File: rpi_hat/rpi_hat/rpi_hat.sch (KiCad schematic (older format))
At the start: 17 parts, among them J1 Raspberry_Pi_2_3, J2 Screw_Terminal_01x02, J3 Screw_Terminal_01x02, J4 Screw_Terminal_01x02, J5 Screw_Terminal_01x02, Q1 2SC1815, Q2 2N7000, U1 L7805

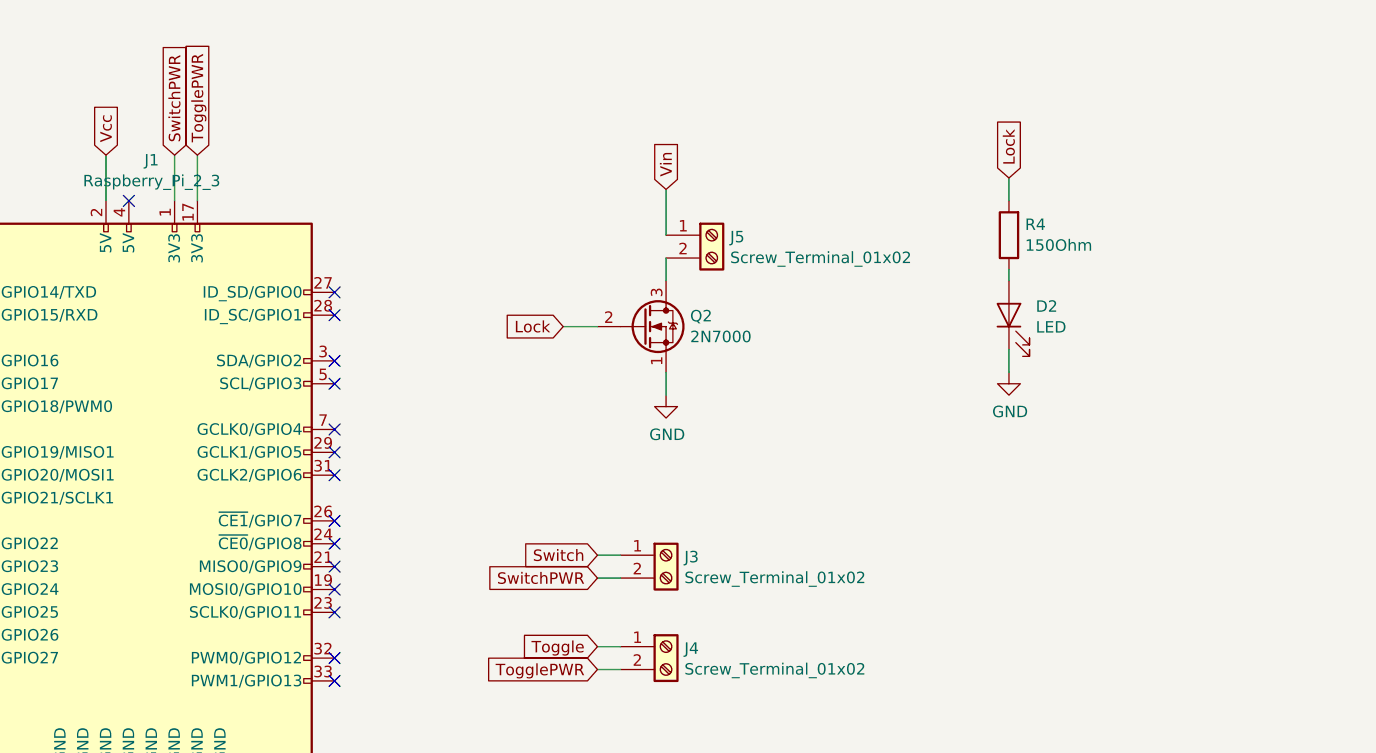
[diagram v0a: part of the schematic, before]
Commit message: Fix pushbutton switch circuit so it doesn't rely on the Pi working
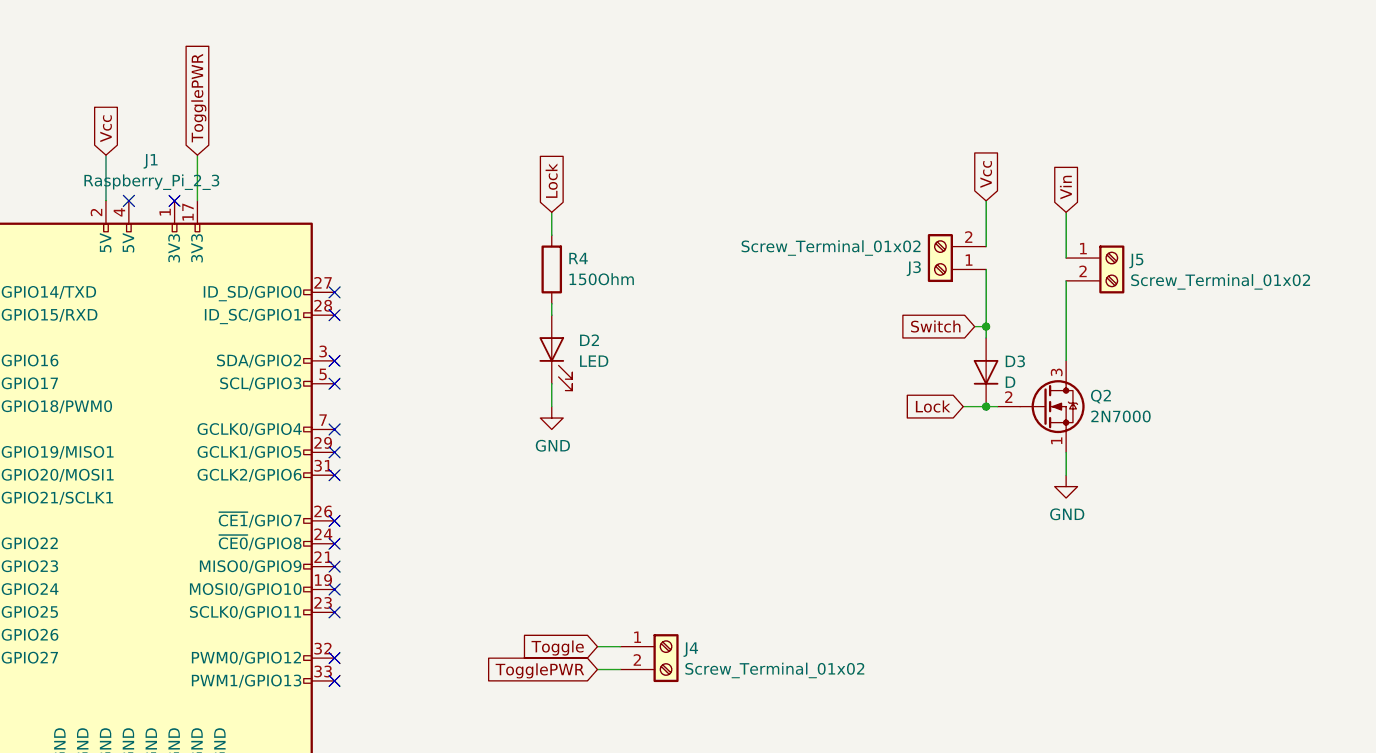
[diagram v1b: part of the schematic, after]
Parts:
- added D3: D, Diodes_SMD:SOD-123, symbol Device:D
- J1: Digikey # (none) -> 1528-1785-ND
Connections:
- net Lock: now also D3.1 (K)
- net Switch: now also D3.2 (A)
- net Vcc: now also J3.2 (Pin_2)
- net SwitchPWR: no longer names the net of J1.1 (3V3)
- net SwitchPWR: no longer J3.2 (Pin_2)
- no-connect marks 25 -> 26
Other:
- moved on the sheet: D2, J3, J5, Q2, R4
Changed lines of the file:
@@
 EESchema Schematic File Version 4
+LIBS:rpi_hat-cache
 EELAYER 26 0
 EELAYER END
@@
 F 2 "Pin_Headers:Pin_Header_Straight_2x20" H 5250 3500 50  0001 C CNN
 F 3 "https://www.raspberrypi.org/documentation/hardware/raspberrypi/schematics/rpi_SCH_3bplus_1p0_reduced.pdf" H 5250 3500 50  0001 C CNN
+F 4 "1528-1785-ND" H 5250 3500 50  0001 C CNN "Digikey #"
 	1    5250 3500
 	1    0    0    -1
@@
 L Transistor_FET:2N7000 Q2
 U 1 1 5C747739
-P 7400 2750
-F 0 "Q2" H 7605 2796 50  0000 L CNN
-F 1 "2N7000" H 7605 2705 50  0000 L CNN
-F 2 "TO_SOT_Packages_THT:TO-220_Neutral123_Horizontal" H 7600 2675 50  0001 L CIN
-F 3 "https://www.fairchildsemi.com/datasheets/2N/2N7000.pdf" H 7400 2750 50  0001 L CNN
-F 4 "497-2779-5-ND" H 7400 2750 50  0001 C CNN "Digikey #"
-	1    7400 2750
-	1    0    0    -1
-$EndComp
-Text GLabel 7050 2750 0    50   Input ~ 0
+P 9150 3100
+F 0 "Q2" H 9355 3146 50  0000 L CNN
+F 1 "2N7000" H 9355 3055 50  0000 L CNN
+F 2 "TO_SOT_Packages_THT:TO-220_Neutral123_Horizontal" H 9350 3025 50  0001 L CIN
+F 3 "https://www.fairchildsemi.com/datasheets/2N/2N7000.pdf" H 9150 3100 50  0001 L CNN
+F 4 "497-2779-5-ND" H 9150 3100 50  0001 C CNN "Digikey #"
+	1    9150 3100
+	1    0    0    -1
+$EndComp
+Text GLabel 8800 3100 0    50   Input ~ 0
 Lock
-Wire Wire Line
-	7050 2750 7200 2750
 Text GLabel 4300 4200 0    50   Input ~ 0
 Lock
 Wire Wire Line
 	4300 4200 4450 4200
-Text GLabel 7500 2150 1    50   Input ~ 0
+Text GLabel 9250 2250 1    50   Input ~ 0
 Vin
 $Comp
 L power:GND #PWR0104
 U 1 1 5C747BD6
-P 7500 3050
-F 0 "#PWR0104" H 7500 2800 50  0001 C CNN
-F 1 "GND" H 7505 2877 50  0000 C CNN
-F 2 "" H 7500 3050 50  0001 C CNN
-F 3 "" H 7500 3050 50  0001 C CNN
-	1    7500 3050
-	1    0    0    -1
-$EndComp
-Wire Wire Line
-	7500 2950 7500 3050
+P 9250 3400
+F 0 "#PWR0104" H 9250 3150 50  0001 C CNN
+F 1 "GND" H 9255 3227 50  0000 C CNN
+F 2 "" H 9250 3400 50  0001 C CNN
+F 3 "" H 9250 3400 50  0001 C CNN
+	1    9250 3400
+	1    0    0    -1
+$EndComp
 $Comp
 L Connector:Screw_Terminal_01x02 J5
 U 1 1 5C747DD7
-P 7700 2350
-F 0 "J5" H 7780 2342 50  0000 L CNN
-F 1 "Screw_Terminal_01x02" H 7780 2251 50  0000 L CNN
-F 2 "Terminal_Blocks:TerminalBlock_Pheonix_MKDS1.5-2pol" H 7700 2350 50  0001 C CNN
-F 3 "~" H 7700 2350 50  0001 C CNN
-F 4 "277-1667-ND" H 7700 2350 50  0001 C CNN "Digikey #"
-	1    7700 2350
-	1    0    0    -1
-$EndComp
-Wire Wire Line
-	7500 2150 7500 2350
-Wire Wire Line
-	7500 2450 7500 2550
-$Comp
-L Connector:Screw_Terminal_01x02 J3
-U 1 1 5C7482A2
-P 7500 3750
-F 0 "J3" H 7580 3742 50  0000 L CNN
-F 1 "Screw_Terminal_01x02" H 7580 3651 50  0000 L CNN
-F 2 "Terminal_Blocks:TerminalBlock_Pheonix_MKDS1.5-2pol" H 7500 3750 50  0001 C CNN
-F 3 "~" H 7500 3750 50  0001 C CNN
-F 4 "277-1667-ND" H 7500 3750 50  0001 C CNN "Digikey #"
-	1    7500 3750
-	1    0    0    -1
-$EndComp
-Text GLabel 7200 3750 0    50   Input ~ 0
-Switch
-Text GLabel 7200 3850 0    50   Input ~ 0
-SwitchPWR
-Wire Wire Line
-	7200 3750 7300 3750
-Wire Wire Line
-	7300 3850 7200 3850
+P 9450 2450
+F 0 "J5" H 9530 2442 50  0000 L CNN
+F 1 "Screw_Terminal_01x02" H 9530 2351 50  0000 L CNN
+F 2 "Terminal_Blocks:TerminalBlock_Pheonix_MKDS1.5-2pol" H 9450 2450 50  0001 C CNN
+F 3 "~" H 9450 2450 50  0001 C CNN
+F 4 "277-1667-ND" H 9450 2450 50  0001 C CNN "Digikey #"
+	1    9450 2450
+	1    0    0    -1
+$EndComp
+Wire Wire Line
+	9250 2250 9250 2450
 Text GLabel 4300 4000 0    50   Input ~ 0
 Switch
 Wire Wire Line
 	4300 4000 4450 4000
-Text GLabel 5350 2000 1    50   Input ~ 0
-SwitchPWR
-Wire Wire Line
-	5350 2200 5350 2000
 $Comp
 L Connector:Screw_Terminal_01x02 J4
@@
 L Device:LED D2
 U 1 1 5C74A07C
-P 9000 2700
-F 0 "D2" V 9038 2583 50  0000 R CNN
-F 1 "LED" V 8947 2583 50  0000 R CNN
-F 2 "LEDs:LED_0603" H 9000 2700 50  0001 C CNN
-F 3 "~" H 9000 2700 50  0001 C CNN
-F 4 "160-1478-1-ND" V 9000 2700 50  0001 C CNN "Digikey #"
-	1    9000 2700
+P 7000 2850
+F 0 "D2" V 7038 2733 50  0000 R CNN
+F 1 "LED" V 6947 2733 50  0000 R CNN
+F 2 "LEDs:LED_0603" H 7000 2850 50  0001 C CNN
+F 3 "~" H 7000 2850 50  0001 C CNN
+F 4 "160-1478-1-ND" V 7000 2850 50  0001 C CNN "Digikey #"
+	1    7000 2850
 	0    -1   -1   0
 $EndComp
@@
 L Device:R R4
 U 1 1 5C74A0F2
-P 9000 2350
-F 0 "R4" H 8930 2304 50  0000 R CNN
-F 1 "150Ohm" H 8930 2395 50  0000 R CNN
-F 2 "Resistors_SMD:R_0603" V 8930 2350 50  0001 C CNN
-F 3 "~" H 9000 2350 50  0001 C CNN
-F 4 "P150DBCT-ND" H 9000 2350 50  0001 C CNN "Digikey #"
-	1    9000 2350
+P 7000 2500
+F 0 "R4" H 6930 2454 50  0000 R CNN
+F 1 "150Ohm" H 6930 2545 50  0000 R CNN
+F 2 "Resistors_SMD:R_0603" V 6930 2500 50  0001 C CNN
+F 3 "~" H 7000 2500 50  0001 C CNN
+F 4 "P150DBCT-ND" H 7000 2500 50  0001 C CNN "Digikey #"
+	1    7000 2500
 	-1   0    0    1
 $EndComp
 Wire Wire Line
-	9000 2550 9000 2500
+	7000 2700 7000 2650
 $Comp
 L power:GND #PWR0105
 U 1 1 5C74B314
-P 9000 2950
-F 0 "#PWR0105" H 9000 2700 50  0001 C CNN
-F 1 "GND" H 9005 2777 50  0000 C CNN
-F 2 "" H 9000 2950 50  0001 C CNN
-F 3 "" H 9000 2950 50  0001 C CNN
-	1    9000 2950
-	1    0    0    -1
-$EndComp
-Wire Wire Line
-	9000 2950 9000 2850
-Text GLabel 9000 2100 1    50   Input ~ 0
+P 7000 3100
+F 0 "#PWR0105" H 7000 2850 50  0001 C CNN
+F 1 "GND" H 7005 2927 50  0000 C CNN
+F 2 "" H 7000 3100 50  0001 C CNN
+F 3 "" H 7000 3100 50  0001 C CNN
+	1    7000 3100
+	1    0    0    -1
+$EndComp
+Wire Wire Line
+	7000 3100 7000 3000
+Text GLabel 7000 2250 1    50   Input ~ 0
 Lock
 Wire Wire Line
-	9000 2100 9000 2200
+	7000 2250 7000 2350
 $Comp
 L Device:Speaker LS1
@@
 NoConn ~ 6050 2600
 NoConn ~ 5150 2200
+Wire Wire Line
+	9250 2550 9250 2900
+NoConn ~ 5350 2200
+$Comp
+L Connector:Screw_Terminal_01x02 J3
+U 1 1 5C7482A2
+P 8700 2500
+F 0 "J3" H 8780 2492 50  0000 L CNN
+F 1 "Screw_Terminal_01x02" H 8780 2401 50  0000 L CNN
+F 2 "Terminal_Blocks:TerminalBlock_Pheonix_MKDS1.5-2pol" H 8700 2500 50  0001 C CNN
+F 3 "~" H 8700 2500 50  0001 C CNN
+F 4 "277-1667-ND" H 8700 2500 50  0001 C CNN "Digikey #"
+	1    8700 2500
+	-1   0    0    1
+$EndComp
+Wire Wire Line
+	9250 3300 9250 3400
+Wire Wire Line
+	8900 2500 8900 2750
+Text GLabel 8850 2750 0    50   Input ~ 0
+Switch
+Wire Wire Line
+	8850 2750 8900 2750
+Text GLabel 8900 2200 1    50   Input ~ 0
+Vcc
+Wire Wire Line
+	8900 2200 8900 2400
+Wire Wire Line
+	8800 3100 8900 3100
+$Comp
+L Device:D D3
+U 1 1 5C76DE1A
+P 8900 2950
+F 0 "D3" V 8946 2871 50  0000 R CNN
+F 1 "D" V 8855 2871 50  0000 R CNN
+F 2 "Diodes_SMD:SOD-123" H 8900 2950 50  0001 C CNN
+F 3 "~" H 8900 2950 50  0001 C CNN
+F 4 "1N4148WTPMSCT-ND" V 8900 2950 50  0001 C CNN "Digikey #"
+	1    8900 2950
+	0    -1   -1   0
+$EndComp
+Wire Wire Line
+	8900 2800 8900 2750
+Connection ~ 8900 2750
+Connection ~ 8900 3100
+Wire Wire Line
+	8900 3100 8950 3100
 $EndSCHEMATC

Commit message: Correct digikey part # for piezo transistor
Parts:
- Q1: Digikey # (none) -> KSC1815YTACT-ND
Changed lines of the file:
@@
 F 2 "TO_SOT_Packages_THT:TO-92_Inline_Wide" H 2000 5075 50  0001 L CIN
 F 3 "https://media.digikey.com/pdf/Data%20Sheets/Toshiba%20PDFs/2SC1815.pdf" H 1800 5150 50  0001 L CNN
+F 4 "KSC1815YTACT-ND" H 1800 5150 50  0001 C CNN "Digikey #"
 	1    1800 5150
 	1    0    0    -1

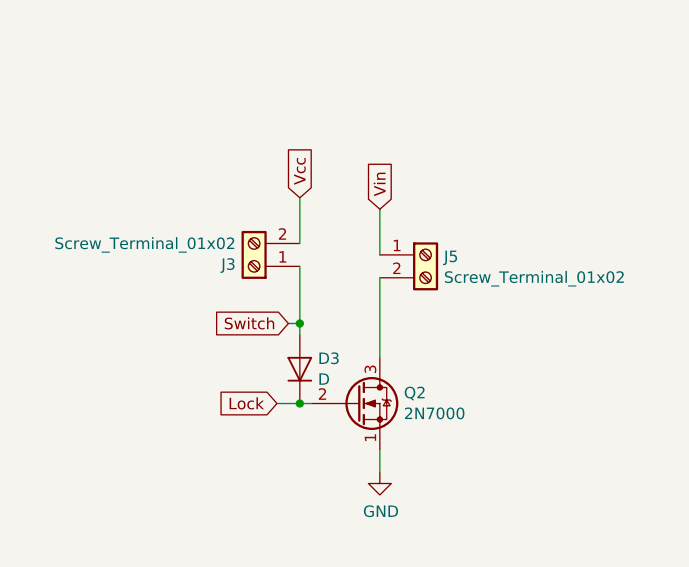
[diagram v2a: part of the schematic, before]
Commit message: Add protection diode
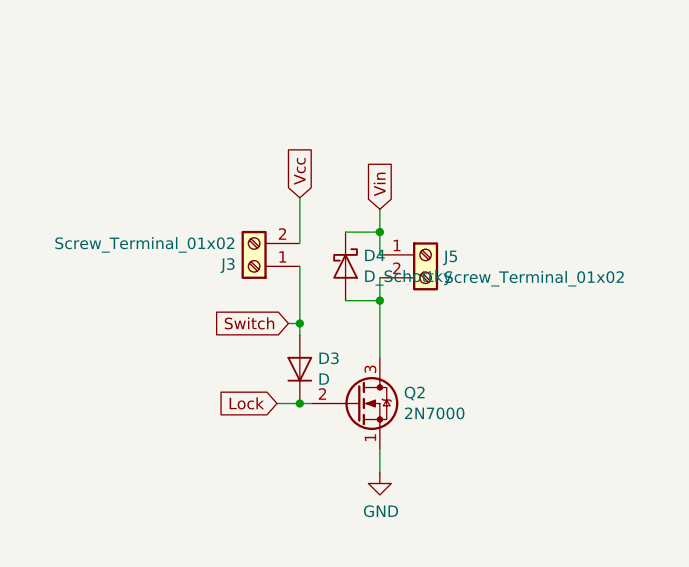
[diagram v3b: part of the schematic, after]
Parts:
- added D4: D_Schottky, Diodes_SMD:SOD-123, symbol Device:D_Schottky
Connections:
- net Vin: now also D4.1 (K)
- net at J5.2 (Pin_2), Q2.3 (D): now also D4.2 (A)
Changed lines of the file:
@@
 $EndComp
 Wire Wire Line
-	9250 2250 9250 2450
+	9250 2250 9250 2350
 Text GLabel 4300 4000 0    50   Input ~ 0
 Switch
@@
 NoConn ~ 5150 2200
 Wire Wire Line
-	9250 2550 9250 2900
+	9250 2550 9250 2650
 NoConn ~ 5350 2200
 $Comp
@@
 Wire Wire Line
 	8900 3100 8950 3100
+$Comp
+L Device:D_Schottky D4
+U 1 1 5C75E921
+P 9100 2500
+F 0 "D4" V 9054 2579 50  0000 L CNN
+F 1 "D_Schottky" V 9145 2579 50  0000 L CNN
+F 2 "Diodes_SMD:SOD-123" H 9100 2500 50  0001 C CNN
+F 3 "~" H 9100 2500 50  0001 C CNN
+F 4 "MBR0540T3GOSCT-ND" V 9100 2500 50  0001 C CNN "Digikey #"
+	1    9100 2500
+	0    1    1    0
+$EndComp
+Wire Wire Line
+	9100 2350 9250 2350
+Connection ~ 9250 2350
+Wire Wire Line
+	9250 2350 9250 2450
+Wire Wire Line
+	9100 2650 9250 2650
+Connection ~ 9250 2650
+Wire Wire Line
+	9250 2650 9250 2900
 $EndSCHEMATC
